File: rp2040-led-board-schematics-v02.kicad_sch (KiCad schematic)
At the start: 36 parts, among them J1 PWR_IN, J13 MainBoard, J5 FrontPanel, SW1 Button, SW2 PEC16, U1 LM7805, U1 Pico, U6 ENC28J60

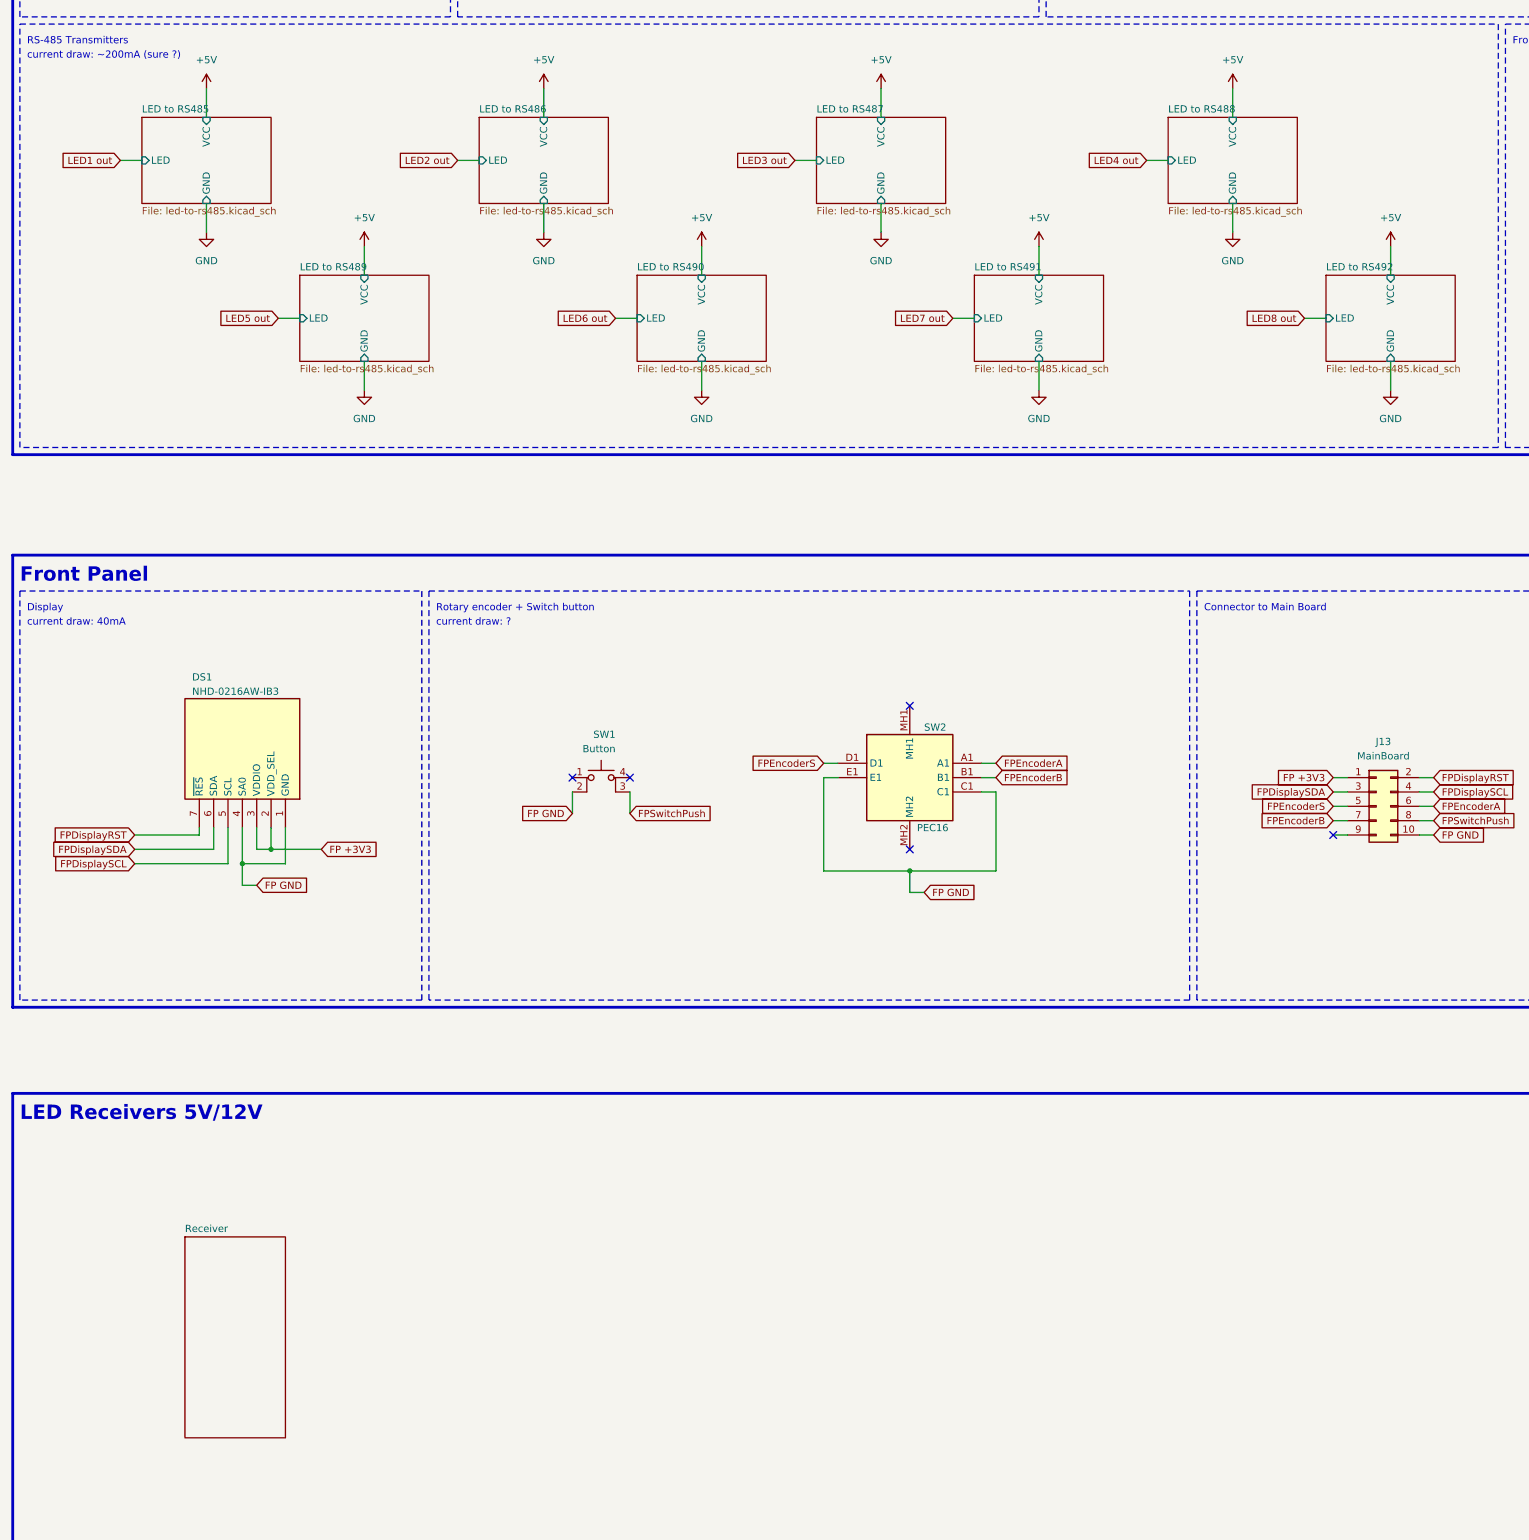
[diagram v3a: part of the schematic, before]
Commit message: receiver layout OK, some references fixed
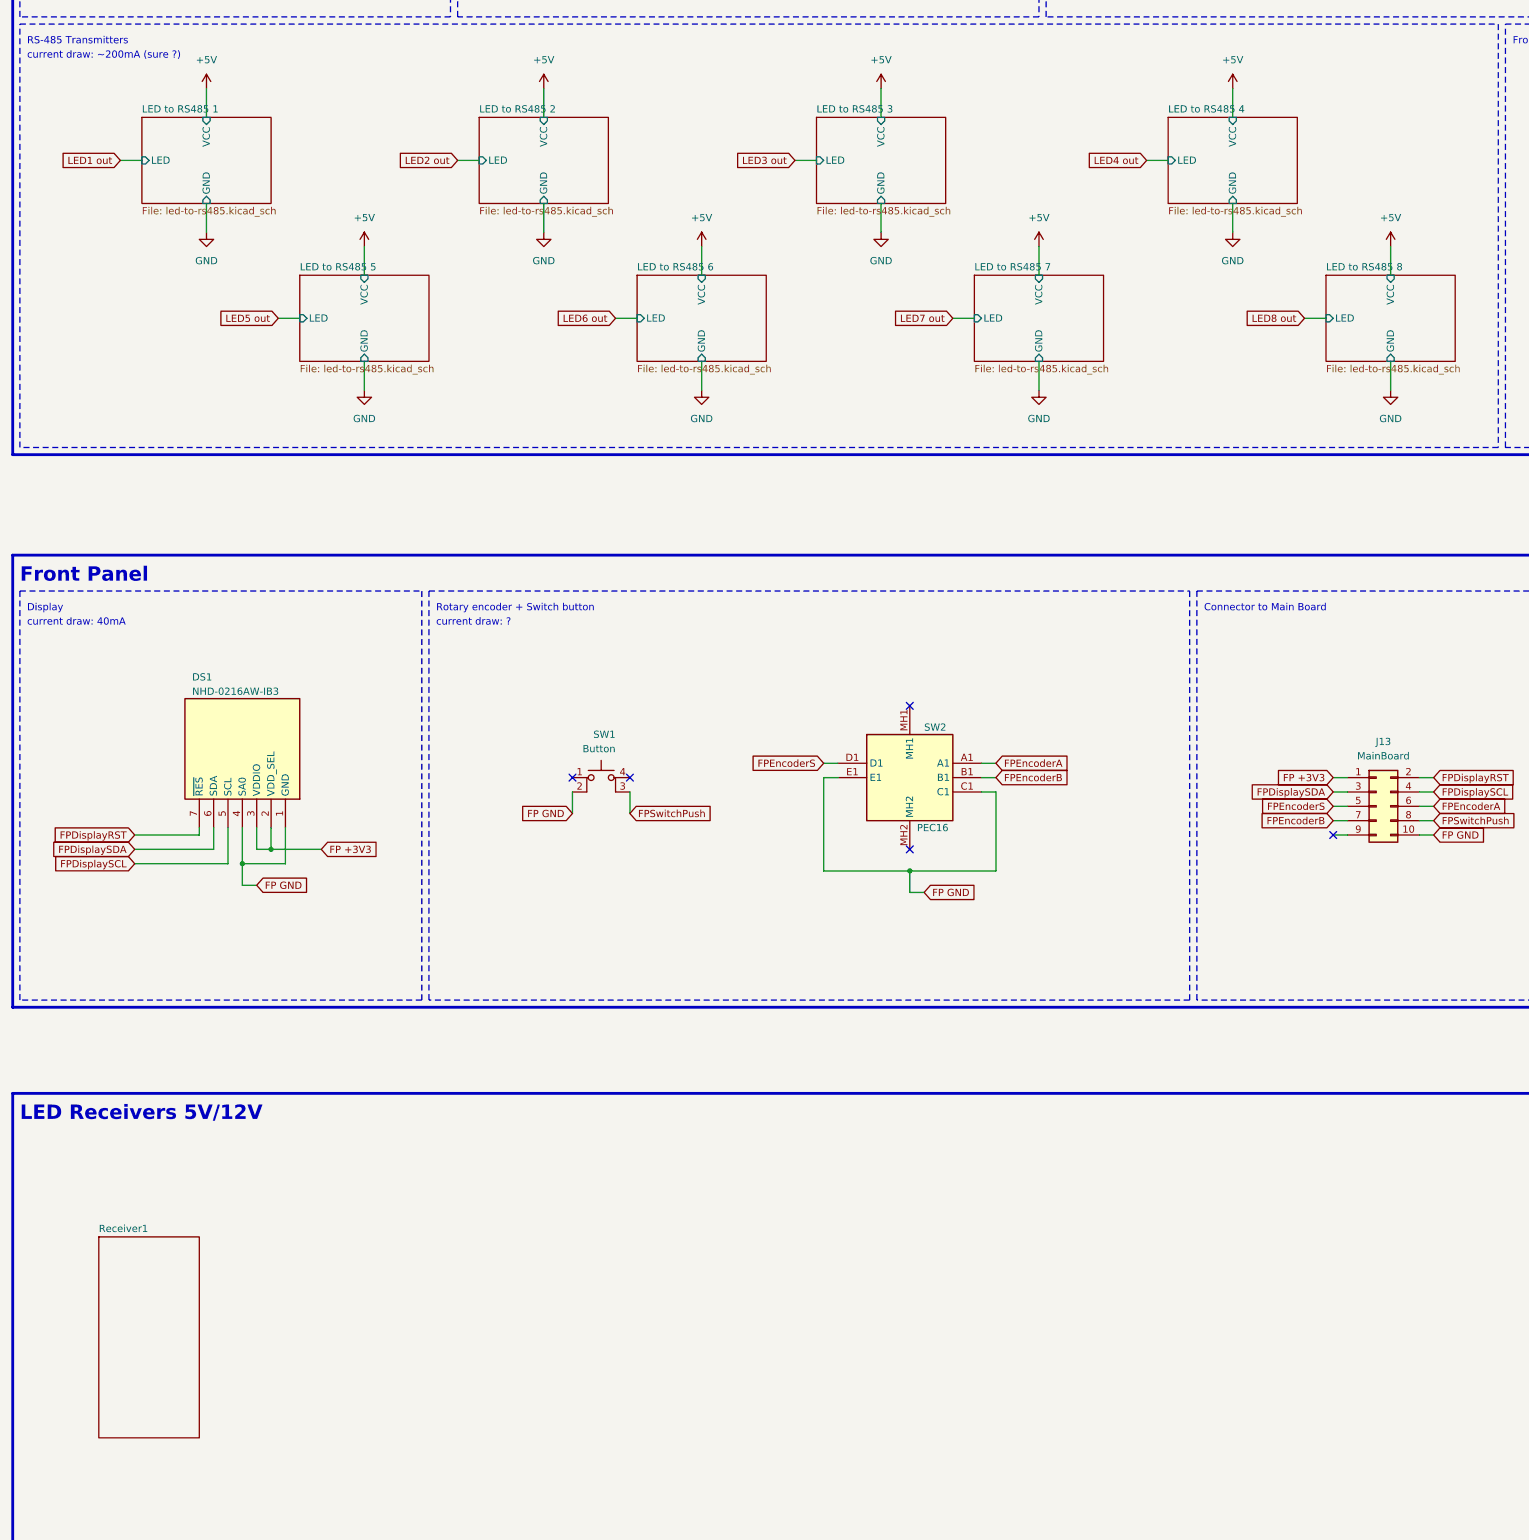
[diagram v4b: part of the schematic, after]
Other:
- sheet LED to RS485 renamed LED to RS485 1
- sheet LED to RS486 renamed LED to RS485 2
- sheet LED to RS487 renamed LED to RS485 3
- sheet LED to RS488 renamed LED to RS485 4
- sheet LED to RS489 renamed LED to RS485 5
- sheet LED to RS490 renamed LED to RS485 6
- sheet LED to RS491 renamed LED to RS485 7
- sheet LED to RS492 renamed LED to RS485 8
- sheet Receiver renamed Receiver1
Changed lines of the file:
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@@
     (stroke (width 0.1524) (type solid))
     (fill (color 255 255 194 1.0000))
-    (property "Sheetname" "LED to RS492" (at 269.24 159.3084 0)
+    (property "Sheetname" "LED to RS485 8" (at 269.24 159.3084 0)
       (effects (font (size 1.27 1.27)) (justify left bottom))
     )
@@
     (stroke (width 0.1524) (type solid))
     (fill (color 255 255 194 1.0000))
-    (property "Sheetname" "LED to RS491" (at 207.01 159.3084 0)
+    (property "Sheetname" "LED to RS485 7" (at 207.01 159.3084 0)
       (effects (font (size 1.27 1.27)) (justify left bottom))
     )
@@
     )
   )
-  (sheet (at 67.31 330.2) (size 17.78 35.56) (fields_autoplaced)
+  (sheet (at 52.07 330.2) (size 17.78 35.56) (fields_autoplaced)
     (stroke (width 0.1524) (type solid))
-    (fill (color 0 0 0 0.0000))
-    (property "Sheetname" "Receiver" (at 67.31 329.4884 0)
+    (fill (color 255 255 194 1.0000))
+    (property "Sheetname" "Receiver1" (at 52.07 329.4884 0)
       (effects (font (size 1.27 1.27)) (justify left bottom))
     )
-    (property "Sheetfile" "Receiver.kicad_sch" (at 67.31 366.3446 0)
+    (property "Sheetfile" "Receiver.kicad_sch" (at 52.07 366.3446 0)
       (effects (font (size 1.27 1.27)) (justify left top) hide)
     )
@@
     (stroke (width 0.1524) (type solid))
     (fill (color 255 255 194 1.0000))
-    (property "Sheetname" "LED to RS488" (at 241.3 131.3684 0)
+    (property "Sheetname" "LED to RS485 4" (at 241.3 131.3684 0)
       (effects (font (size 1.27 1.27)) (justify left bottom))
     )
@@
     (stroke (width 0.1524) (type solid))
     (fill (color 255 255 194 1.0000))
-    (property "Sheetname" "LED to RS487" (at 179.07 131.3684 0)
+    (property "Sheetname" "LED to RS485 3" (at 179.07 131.3684 0)
       (effects (font (size 1.27 1.27)) (justify left bottom))
     )
@@
     (stroke (width 0.1524) (type solid))
     (fill (color 255 255 194 1.0000))
-    (property "Sheetname" "LED to RS485" (at 59.69 131.3684 0)
+    (property "Sheetname" "LED to RS485 1" (at 59.69 131.3684 0)
       (effects (font (size 1.27 1.27)) (justify left bottom))
     )
@@
     (stroke (width 0.1524) (type solid))
     (fill (color 255 255 194 1.0000))
-    (property "Sheetname" "LED to RS486" (at 119.38 131.3684 0)
+    (property "Sheetname" "LED to RS485 2" (at 119.38 131.3684 0)
       (effects (font (size 1.27 1.27)) (justify left bottom))
     )
     (property "Sheetfile" "led-to-rs485.kicad_sch" (at 119.38 147.9046 0)
       (effects (font (size 1.27 1.27)) (justify left top))
+    )
+    (property "Field2" "" (at 119.38 132.08 0)
+      (effects (font (size 1.27 1.27)) hide)
     )
     (pin "LED" input (at 119.38 139.7 180)
@@
     (stroke (width 0.1524) (type solid))
     (fill (color 255 255 194 1.0000))
-    (property "Sheetname" "LED to RS490" (at 147.32 159.3084 0)
+    (property "Sheetname" "LED to RS485 6" (at 147.32 159.3084 0)
       (effects (font (size 1.27 1.27)) (justify left bottom))
     )
@@
     (stroke (width 0.1524) (type solid))
     (fill (color 255 255 194 1.0000))
-    (property "Sheetname" "LED to RS489" (at 87.63 159.3084 0)
+    (property "Sheetname" "LED to RS485 5" (at 87.63 159.3084 0)
       (effects (font (size 1.27 1.27)) (justify left bottom))
     )

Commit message: OK for first fabrication review
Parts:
- added FM4: Fiducial, Fiducial:Fiducial_1mm_Mask2mm, symbol Mechanical:Fiducial
- added H25, H26, H27, H28: MountingHole, MountingHole:MountingHole_2mm, symbol Mechanical:MountingHole
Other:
- sheet Receiver1 renamed Receiver 1
- added sheet Receiver 2 (Receiver.kicad_sch)
- added sheet Receiver 3 (Receiver.kicad_sch)
- added sheet Receiver 4 (Receiver.kicad_sch)
- added sheet Receiver 5 (Receiver.kicad_sch)
- added sheet Receiver 6 (Receiver.kicad_sch)
- added sheet Receiver 7 (Receiver.kicad_sch)
- added sheet Receiver 8 (Receiver.kicad_sch)
- note added: "Panelization"
- moved on the sheet: FM1, FM2, FM3

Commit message: panelization with only mouse bites, routing finished
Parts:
- added H29, H30, H31, H32, H33, H34: ~, Library:mouse-bites-1x07-jlc, symbol Library:mouse-bites-1x07-jlc
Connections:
- net +3V3: now also J5.10 (Pin_10); no longer J5.1 (Pin_1)
- net FP +3V3: now also J13.10 (Pin_10); no longer J13.1 (Pin_1)
- net FP GND: now also J13.1 (Pin_1), SW1.1; no longer J13.10 (Pin_10)
- net FPDisplayRST: now also J13.9 (Pin_9); no longer J13.2 (Pin_2)
- net FPDisplaySCL: now also J13.7 (Pin_7); no longer J13.4 (Pin_4)
- net FPDisplaySDA: now also J13.8 (Pin_8); no longer J13.3 (Pin_3)
- net FPEncoderA: now also J13.5 (Pin_5); no longer J13.6 (Pin_6)
- net FPEncoderB: now also J13.4 (Pin_4); no longer J13.7 (Pin_7)
- net FPEncoderS: now also J13.6 (Pin_6); no longer J13.5 (Pin_5)
- net FPSwitchPush: now also J13.3 (Pin_3), SW1.4 (A); no longer J13.8 (Pin_8)
- net GND: now also J5.1 (Pin_1); no longer J5.10 (Pin_10)
- net MBEncoderA: now also J5.5 (Pin_5); no longer J5.6 (Pin_6)
- net MBEncoderB: now also J5.4 (Pin_4); no longer J5.7 (Pin_7)
- net MBEncoderS: now also J5.6 (Pin_6); no longer J5.5 (Pin_5)
- net MBSwitchPush: now also J5.3 (Pin_3); no longer J5.8 (Pin_8)
- net MCUDisplayRST: now also J5.9 (Pin_9); no longer J5.2 (Pin_2)
- net MCUDisplaySCL: now also J5.7 (Pin_7); no longer J5.4 (Pin_4)
- net MCUDisplaySDA: now also J5.8 (Pin_8); no longer J5.3 (Pin_3)
- no-connect marks 25 -> 23

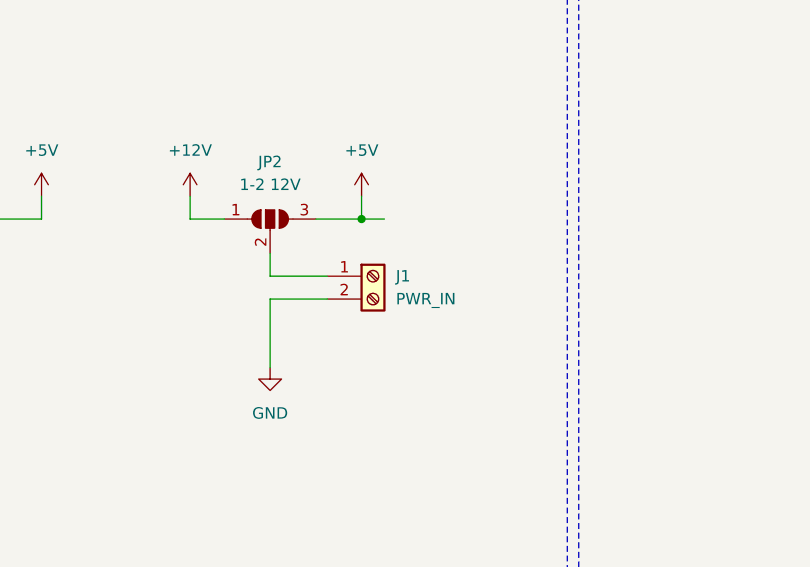
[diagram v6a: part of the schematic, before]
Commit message: resize front panel, fix header orientation, fix receivers layouts and footprints
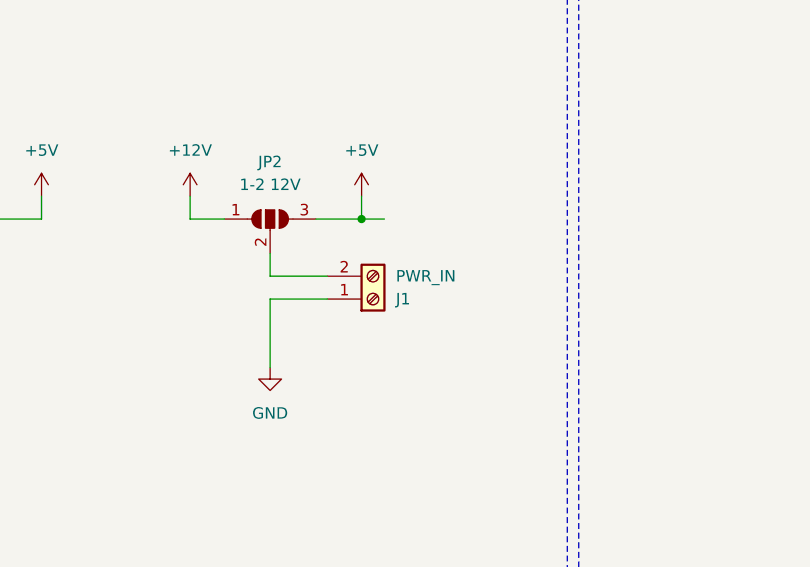
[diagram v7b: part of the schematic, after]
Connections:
- net GND: now also J1.1 (Pin_1); no longer J1.2 (Pin_2)
- net at JP2.2 (C): now also J1.2 (Pin_2); no longer J1.1 (Pin_1)
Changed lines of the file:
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@@
+    )
+  )
+  (symbol (lib_id "Connector:Screw_Terminal_01x02") (at 320.04 81.28 0) (mirror x) (unit 1)
+    (in_bom yes) (on_board yes) (dnp no)
+    (property "Reference" "J1" (at 322.58 81.28 0)
+      (effects (font (size 1.27 1.27)) (justify left))
+    )
+    (property "Value" "PWR_IN" (at 322.58 78.74 0)
+      (effects (font (size 1.27 1.27)) (justify left))
+    )
+    (property "Footprint" "Frangitron:ScrewTerminal_01x02_5.08_Amphenol" (at 320.04 81.28 0)
+      (effects (font (size 1.27 1.27)) hide)
+    )
+    (property "Datasheet" "~" (at 320.04 81.28 0)
+      (effects (font (size 1.27 1.27)) hide)
+    )
+    (property "URL" "https://www.mouser.fr/ProductDetail/Amphenol-Anytek/VI0221550000G?qs=Mv7BduZupUiO9qU7CMoDww%3D%3D" (at 320.04 81.28 0)
+      (effects (font (size 1.27 1.27)) hide)
+    )
+    (pin "1")
+    (pin "2")
+    (instances
+      (project "rp2040-led-board-schematics-v02"
+        (path "/c1a38541-3f06-4b3b-ba3a-decae3ac3c31"
+          (reference "J1") (unit 1)
+        )
+      )
     )
   )
@@
         )
       )
-    )
-  )
-  (symbol (lib_id "Connector:Screw_Terminal_01x02") (at 320.04 78.74 0) (unit 1)
-    (in_bom yes) (on_board yes) (dnp no) (fields_autoplaced)
-    (property "Reference" "J1" (at 322.58 78.74 0)
-      (effects (font (size 1.27 1.27)) (justify left))
-    )
-    (property "Value" "PWR_IN" (at 322.58 81.28 0)
-      (effects (font (size 1.27 1.27)) (justify left))
-    )
-    (property "Footprint" "Frangitron:ScrewTerminal_01x02_5.08_Amphenol" (at 320.04 78.74 0)
-      (effects (font (size 1.27 1.27)) hide)
-    )
-    (property "Datasheet" "~" (at 320.04 78.74 0)
-      (effects (font (size 1.27 1.27)) hide)
-    )
-    (property "URL" "https://www.mouser.fr/ProductDetail/Amphenol-Anytek/VI0221550000G?qs=Mv7BduZupUiO9qU7CMoDww%3D%3D" (at 320.04 78.74 0)
-      (effects (font (size 1.27 1.27)) hide)
-    )
-    (pin "1")
-    (pin "2")
-    (instances
-      (project "rp2040-led-board-schematics-v02"
-        (path "/c1a38541-3f06-4b3b-ba3a-decae3ac3c31"
-          (reference "J1") (unit 1)
-        )
-      )

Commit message: Geographically reannotate
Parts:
- DS1: footprint NHD0216AWIB3 -> Frangitron:NewHaven-OLED-NHD-0216AW-IB3
- SW1: renamed from SW2; footprint PEC164120FS0012 -> SamacSys_Parts:PEC164120FS0012
- U1: footprint RPi_Pico:RPi_Pico_SMD_TH -> MCU_RaspberryPi_and_Boards:RPi_Pico_SMD_TH
- U6: footprint Frangitron:ENC28J60_module -> Library:ENC28J60-SPI-Ethernet-Module
- renumbered C12 to C33, C13 to C34, C11 to C35, C22 to C36, FM4 to FM3, FM3 to FM4, H25 to H1, H1 to H10, H2 to H11, H8 to H12, H28 to H2, H4 to H22, H5 to H23, H9 to H24, H33 to H25, H34 to H26, H29 to H27, H31 to H3, H26 to H32, H27 to H33, H32 to H4, H30 to H5, J13 to J27, J1 to J5, J5 to J9, JP2 to JP10, JP1 to JP5, R24 to R52, R25 to R53, R1 to R54, R20 to R55, R23 to R56, R22 to R57, R21 to R58, R19 to R59, SW1 to SW2, U1 to U5
